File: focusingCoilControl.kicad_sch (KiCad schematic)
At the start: 20 parts

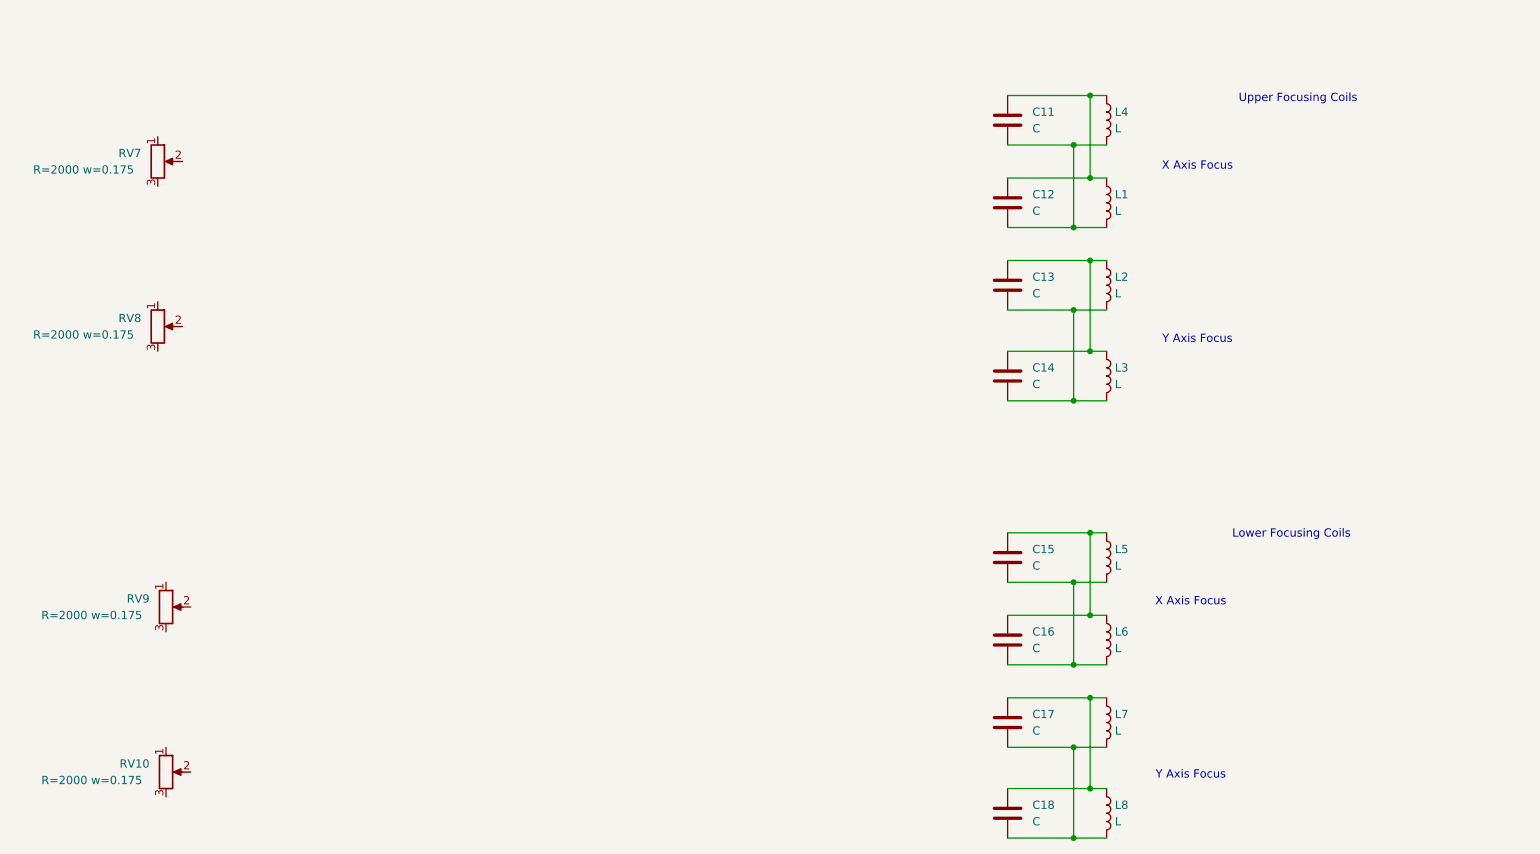
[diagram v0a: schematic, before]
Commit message: added more untested ideas for schematics
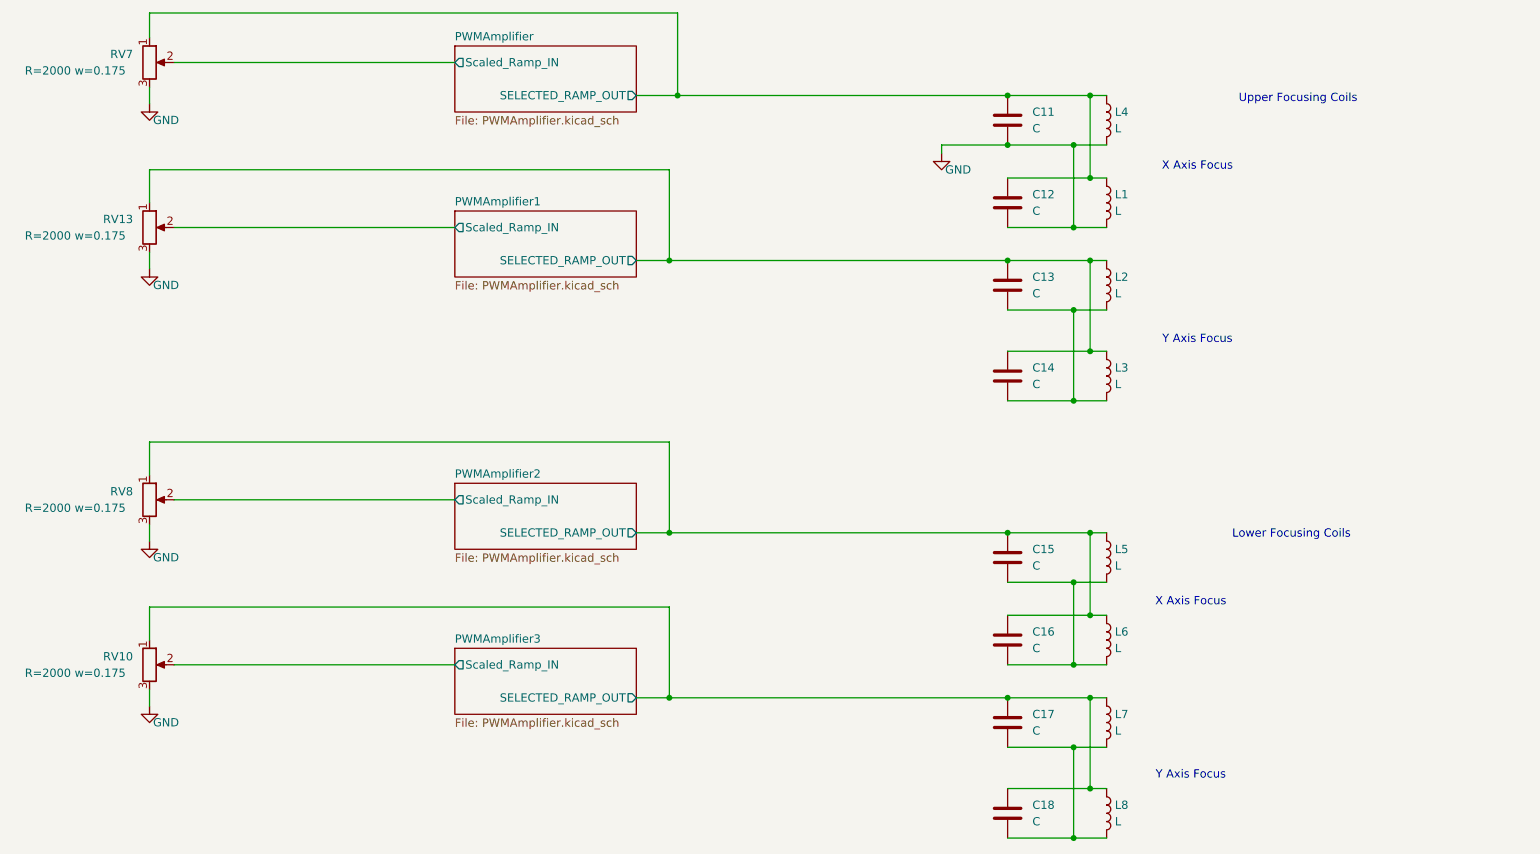
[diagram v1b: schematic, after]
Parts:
- removed RV9: 2M, Potentiometer_SMD:Potentiometer_Bourns_TC33X_Vertical, symbol Device:R_Potentiometer
- added RV13: 2M, Potentiometer_SMD:Potentiometer_Bourns_TC33X_Vertical, symbol Device:R_Potentiometer
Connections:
- net PWMAmplifier3/SELECTED_RAMP_OUT: now reaches C17.1, C18.1, L7.1, L8.1
- net PWMAmplifier3/SELECTED_RAMP_OUT: now also RV10.1
- net PWMAmplifier/SELECTED_RAMP_OUT: now reaches C11.1, C12.1, L1.1, L4.1
- net PWMAmplifier/SELECTED_RAMP_OUT: now also RV7.1
- net GND: now reaches C11.2, C12.2, L1.2, L4.2
- net GND: now also RV10.3, RV7.3, RV8.3, RV13.3
- net PWMAmplifier2/SELECTED_RAMP_OUT: now reaches C15.1, C16.1, L5.1, L6.1
- net PWMAmplifier2/SELECTED_RAMP_OUT: now also RV8.1
- net PWMAmplifier1/SELECTED_RAMP_OUT: now reaches C13.1, C14.1, L2.1, L3.1
- net PWMAmplifier1/SELECTED_RAMP_OUT: now also RV13.1
- net PWMAmplifier3/Scaled_Ramp_IN: now reaches RV10.2
- net PWMAmplifier2/Scaled_Ramp_IN: now reaches RV8.2
- net PWMAmplifier/Scaled_Ramp_IN: now reaches RV7.2
- new net PWMAmplifier1/Scaled_Ramp_IN: RV13.2
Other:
- added sheet PWMAmplifier (PWMAmplifier.kicad_sch)
- added sheet PWMAmplifier1 (PWMAmplifier.kicad_sch)
- added sheet PWMAmplifier2 (PWMAmplifier.kicad_sch)
- added sheet PWMAmplifier3 (PWMAmplifier.kicad_sch)
- moved on the sheet: RV7

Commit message: linked models so spice simulation runs
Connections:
- net GND: now also C13.2, C14.2, C15.2, C16.2, C17.2, C18.2, L2.2, L3.2, L5.2, L6.2, L7.2, L8.2
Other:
- moved on the sheet: RV10, RV13, RV7, RV8

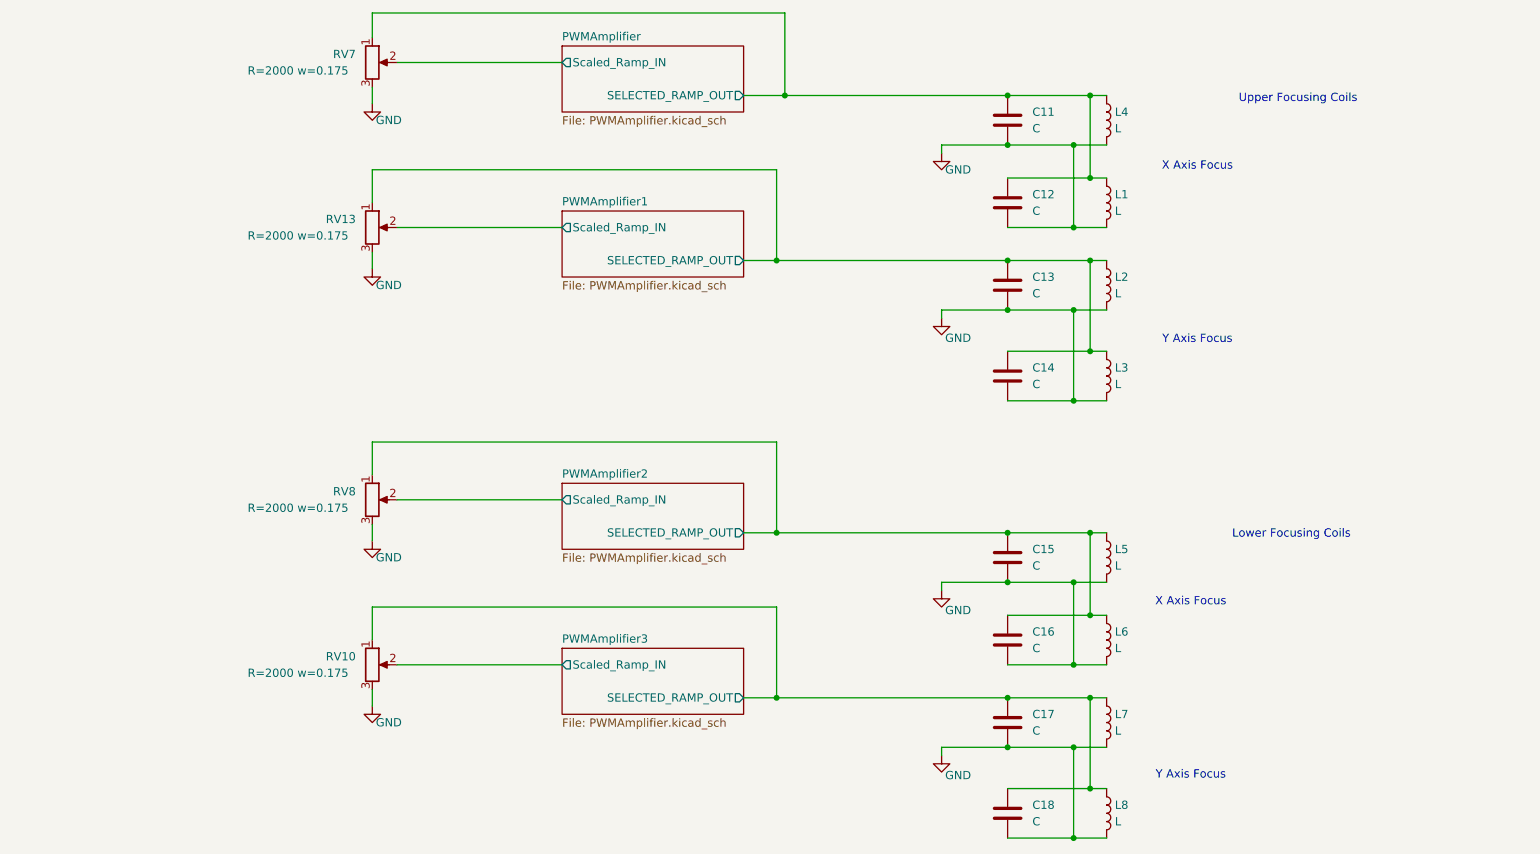
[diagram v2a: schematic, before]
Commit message: added new spice directives to improve simulation speed, added sections for motor drivers, micro controlers, i2c bus connections, realized that focusing coils, hv, horizontal and vertical ramp will need time stable signals (not voltage dependant like with a voltage controlled oscilator) so it will be much simpler to design them with micro controllers
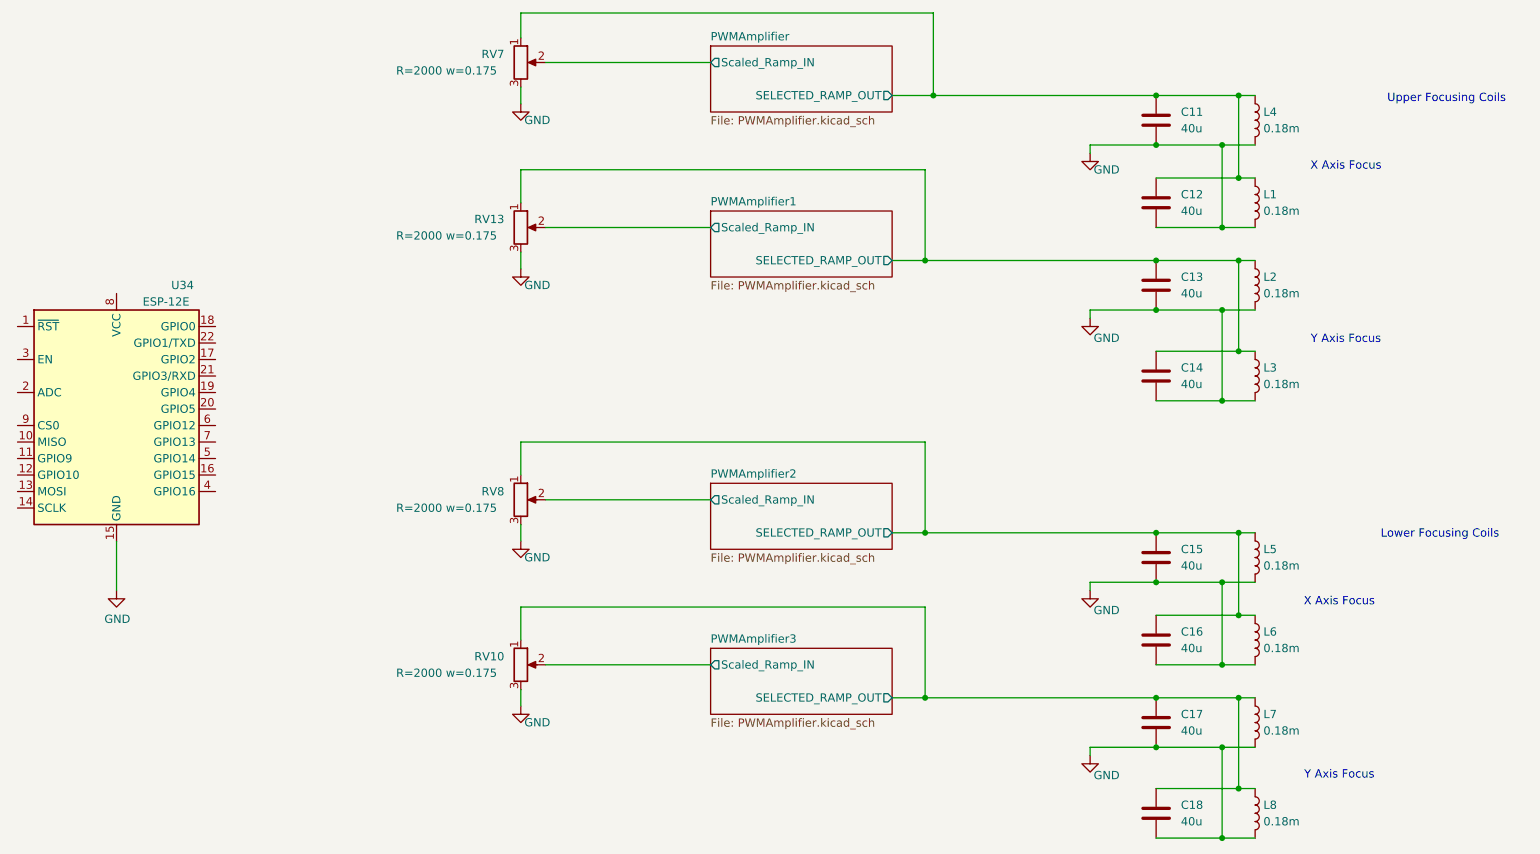
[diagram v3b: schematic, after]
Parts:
- added U34: ESP-12E, RF_Module:ESP-12E, symbol RF_Module:ESP-12E
- C11, C12, C13, C14, C15, C16, C17, C18: value C -> 40u
- L1, L2, L3, L4, L5, L6, L7, L8: value L -> 0.18m
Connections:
- net GND: now also U34.15 (GND)
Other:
- moved on the sheet: C11, C12, C13, C14, C15, C16, C17, C18, L1, L2, L3, L4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

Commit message: changed bldc driver schematic to use esp32 devkit
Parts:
- C11, C12, C13, C14, C15, C16, C17, C18: footprint (none) -> Capacitor_SMD:C_1206_3216Metric
- L1: footprint (none) -> crtDriver:ESP32-DOIT-DEVKIT
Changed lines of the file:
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@@
 			)
 		)
-		(property "Footprint" ""
+		(property "Footprint" "Capacitor_SMD:C_1206_3216Metric"
 			(at 211.7852 148.59 0)
 			(effects
@@
 			)
 		)
-		(property "Footprint" ""
+		(property "Footprint" "Capacitor_SMD:C_1206_3216Metric"
 			(at 211.7852 54.61 0)
 			(effects
@@
 			)
 		)
-		(property "Footprint" ""
+		(property "Footprint" "Capacitor_SMD:C_1206_3216Metric"
 			(at 211.7852 121.92 0)
 			(effects
@@
 			)
 		)
-		(property "Footprint" ""
+		(property "Footprint" "Capacitor_SMD:C_1206_3216Metric"
 			(at 211.7852 109.22 0)
 			(effects
@@
 			)
 		)
-		(property "Footprint" ""
+		(property "Footprint" "crtDriver:ESP32-DOIT-DEVKIT"
 			(at 226.06 50.8 0)
 			(effects
@@
 			)
 		)
-		(property "Footprint" ""
+		(property "Footprint" "Capacitor_SMD:C_1206_3216Metric"
 			(at 211.7852 134.62 0)
 			(effects
@@
 			)
 		)
-		(property "Footprint" ""
+		(property "Footprint" "Capacitor_SMD:C_1206_3216Metric"
 			(at 211.7852 67.31 0)
 			(effects
@@
 			)
 		)
-		(property "Footprint" ""
+		(property "Footprint" "Capacitor_SMD:C_1206_3216Metric"
 			(at 211.7852 41.91 0)
 			(effects
@@
 			)
 		)
-		(property "Footprint" ""
+		(property "Footprint" "Capacitor_SMD:C_1206_3216Metric"
 			(at 211.7852 81.28 0)
 			(effects

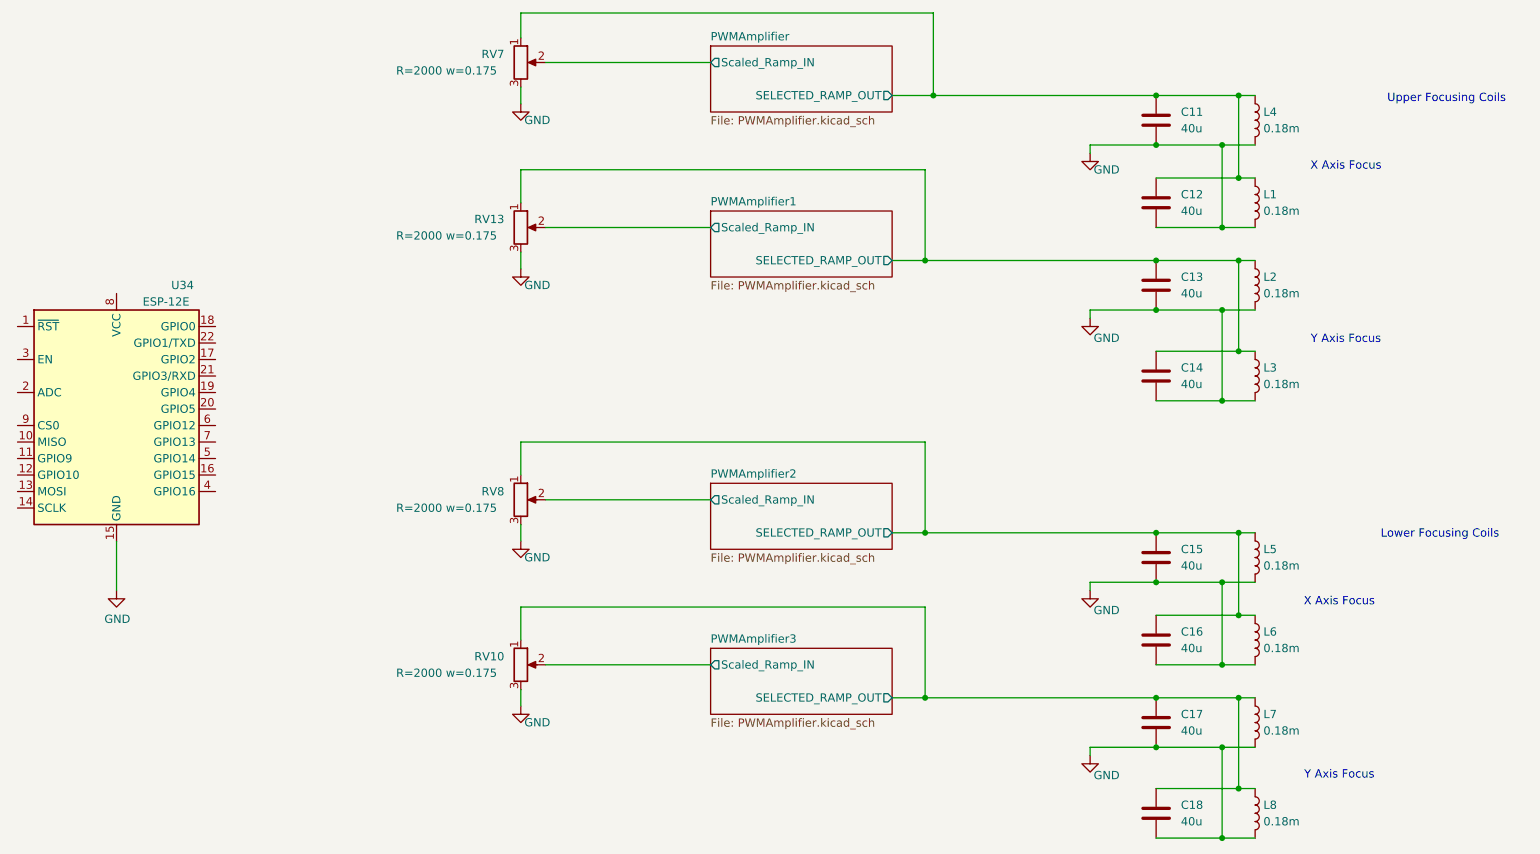
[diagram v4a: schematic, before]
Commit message: added sections to add to overview schematic, added some of the component schematics
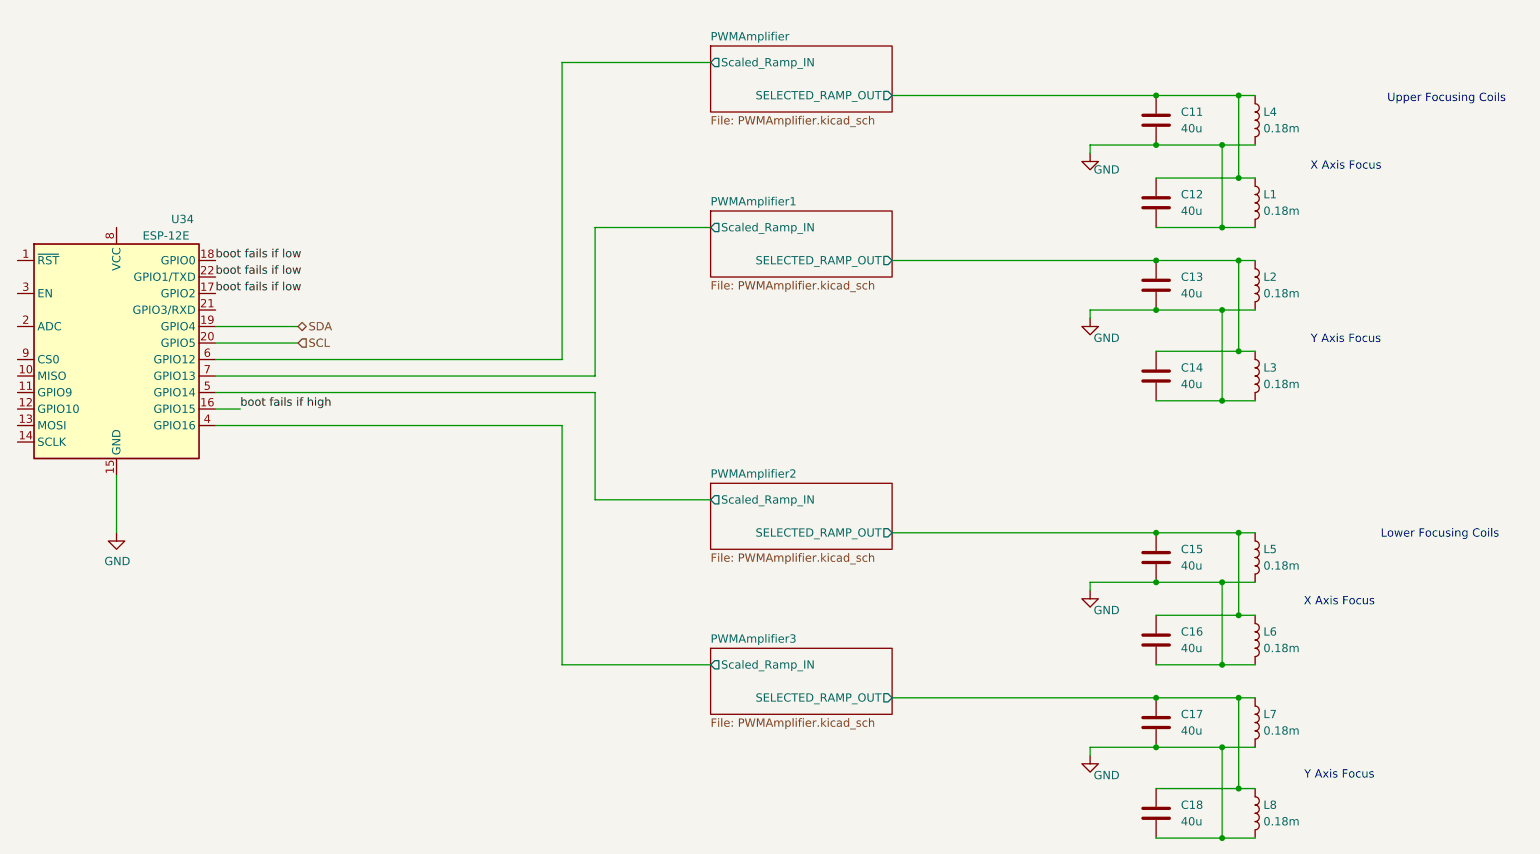
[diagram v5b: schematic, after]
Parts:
- removed RV10, RV13, RV7, RV8: 2M, Potentiometer_SMD:Potentiometer_Bourns_TC33X_Vertical, symbol Device:R_Potentiometer
- L1: footprint crtDriver:ESP32-DOIT-DEVKIT -> (none)
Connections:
- net PWMAmplifier/Scaled_Ramp_IN: now also U34.6 (GPIO12)
- net PWMAmplifier1/Scaled_Ramp_IN: now also U34.7 (GPIO13)
- net PWMAmplifier2/Scaled_Ramp_IN: now also U34.5 (GPIO14)
- net PWMAmplifier3/Scaled_Ramp_IN: now also U34.4 (GPIO16)
- net boot fails if high: now reaches U34.16 (GPIO15)
- net boot fails if low: now reaches U34.17 (GPIO2)
- net boot fails if low: now also U34.18 (GPIO0), U34.22 (GPIO1/TXD)
- net SDA: now reaches U34.19 (GPIO4)
- net SCL: now reaches U34.20 (GPIO5)
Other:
- moved on the sheet: U34
